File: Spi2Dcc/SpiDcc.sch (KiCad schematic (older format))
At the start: 0 parts

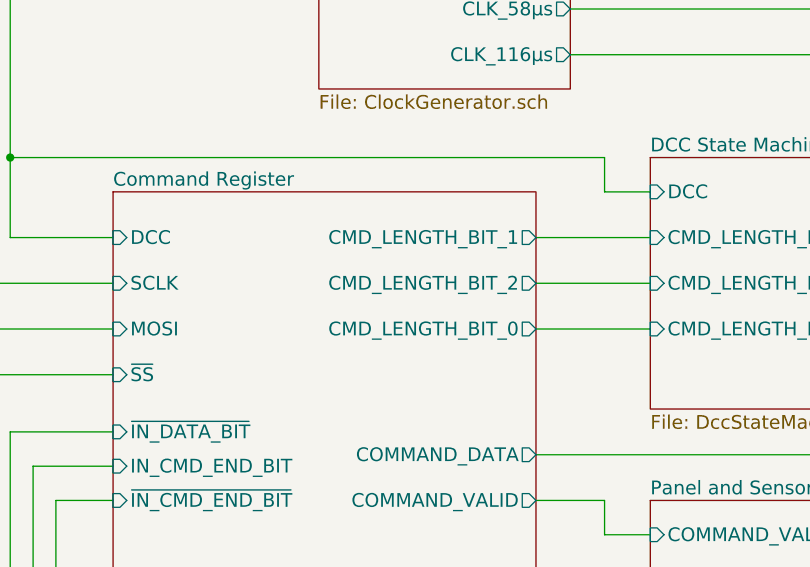
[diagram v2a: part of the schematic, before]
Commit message: fix command length bits swapped. Connect mounting hole pads to GND.
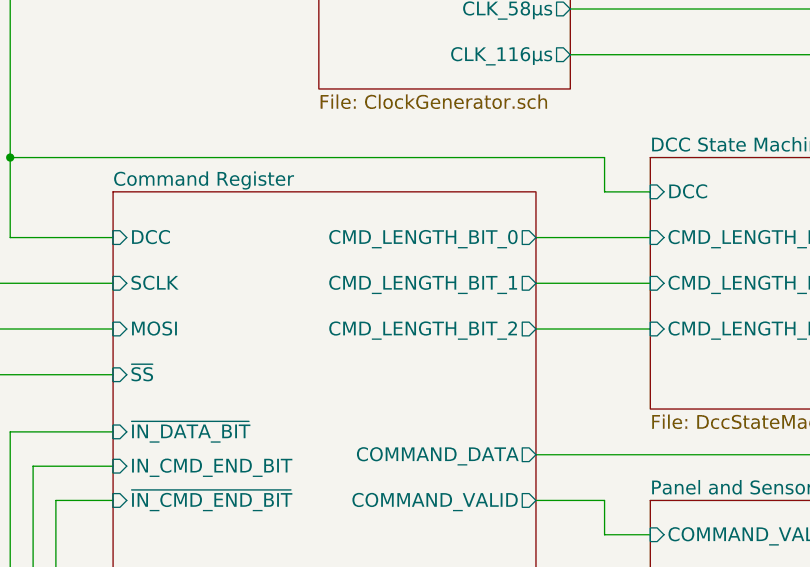
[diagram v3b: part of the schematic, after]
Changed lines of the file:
@@
 F3 "~IN_DATA_BIT~" I L 2850 4450 60
 F4 "~IN_CMD_END_BIT~" I L 2850 4750 60
-F5 "CMD_LENGTH_BIT_0" O R 4700 4000 60
-F6 "CMD_LENGTH_BIT_1" O R 4700 3600 60
-F7 "CMD_LENGTH_BIT_2" O R 4700 3800 60
+F5 "CMD_LENGTH_BIT_0" O R 4700 3600 60
+F6 "CMD_LENGTH_BIT_1" O R 4700 3800 60
+F7 "CMD_LENGTH_BIT_2" O R 4700 4000 60
 F8 "COMMAND_DATA" O R 4700 4550 60
 F9 "IN_CMD_END_BIT" I L 2850 4600 60
